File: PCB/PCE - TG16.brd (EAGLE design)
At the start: 58.5 x 60.9 mm, 13 parts, among them U1 SN74AHCT125N, U2 SN74AHCT125N

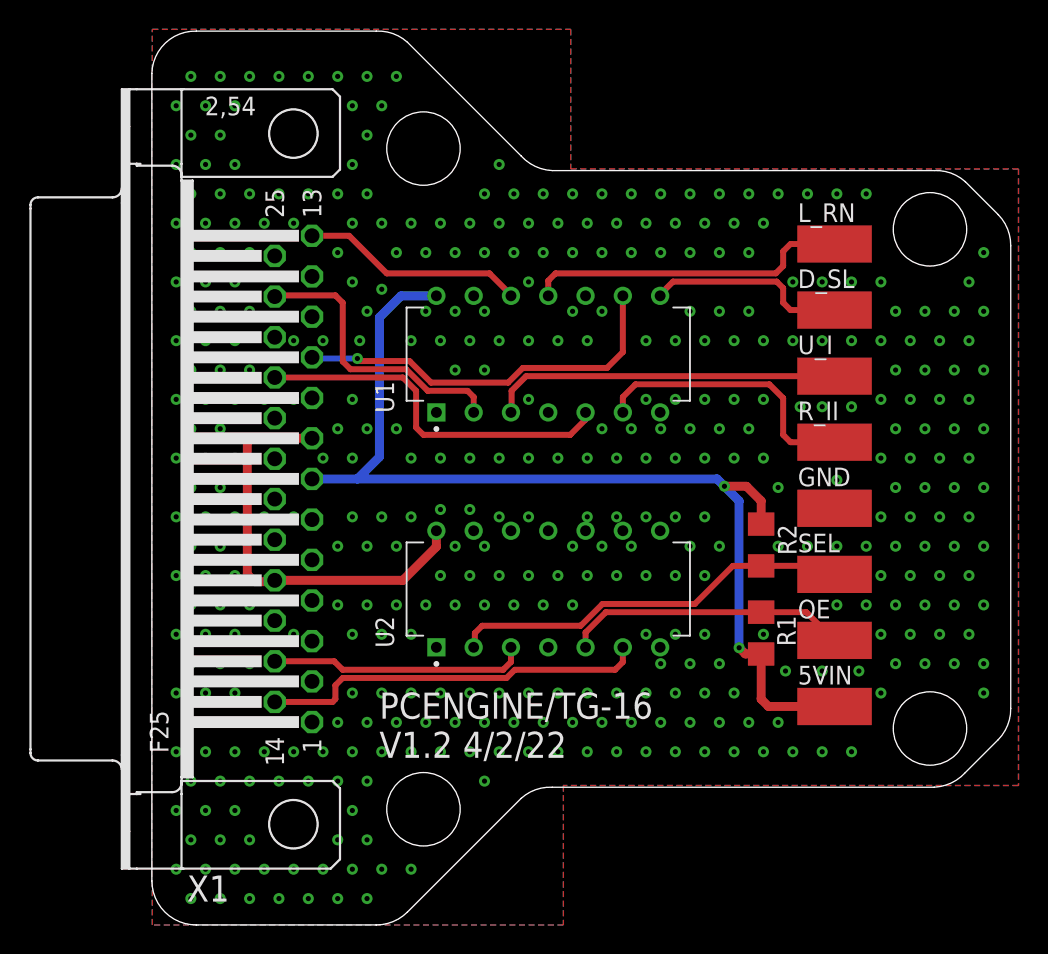
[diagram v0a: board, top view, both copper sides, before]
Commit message: Added exposed GND plane at DB25 anchors
All PCBs have been update to have exposed GND plane pads for the DB25 anchor points.

This resolves Issue 54
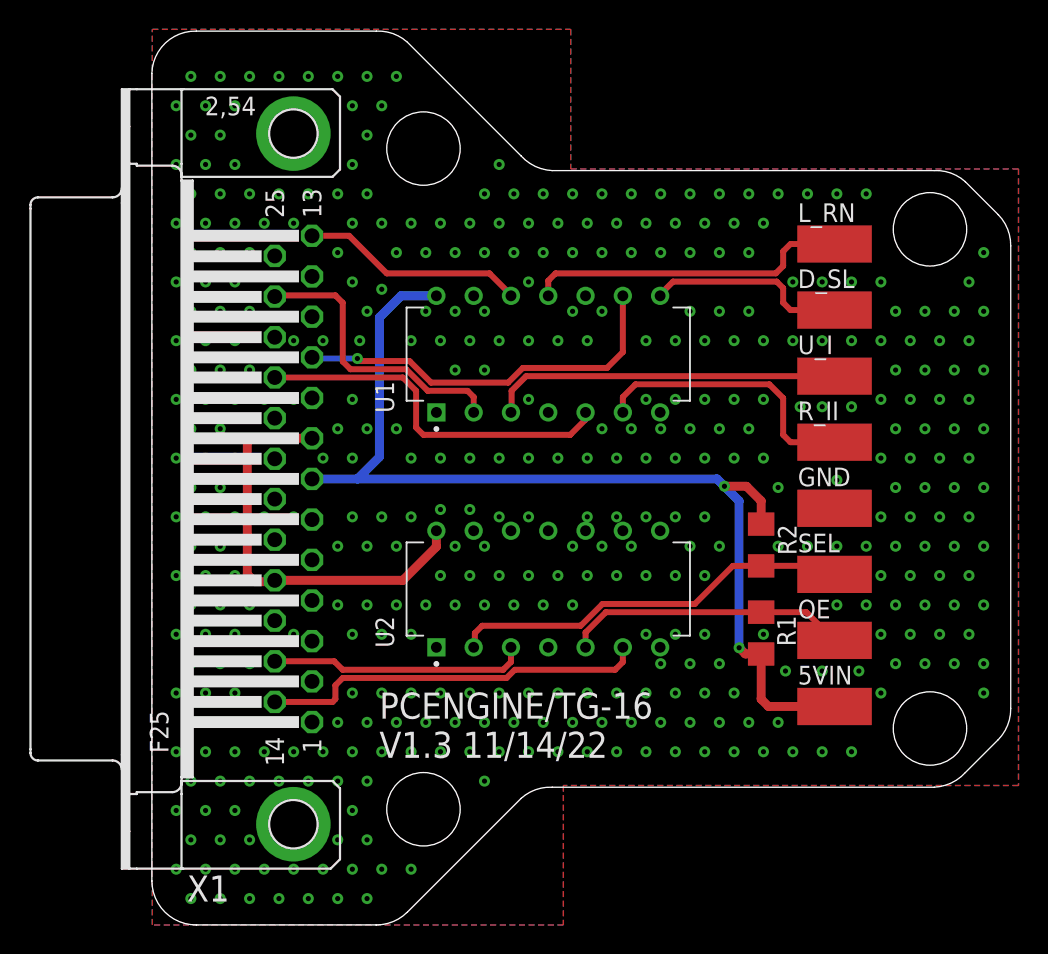
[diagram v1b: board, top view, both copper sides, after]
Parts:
- X1: device SparkFun-Retired:F25H -> SparkFun-Retired:F25HP
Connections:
- net GND: now also X1.GND1, X1.GND2
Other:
- board text added: "PCENGINE/TG-16 V1.3 11/14/22"
- board text removed: "PCENGINE/TG-16 V1.2 4/2/22"
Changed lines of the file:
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@@
 <hole x="18.5" y="8" drill="5"/>
 <text x="15.5" y="11.5" size="1.778" layer="21">PCENGINE/TG-16
-V1.2 4/2/22</text>
+V1.3 11/14/22</text>
 </plain>
 <attributes>
@@
 <attribute name="PURCHASE-URL" value="https://pricing.snapeda.com/search/part/SN74AHCT125N/?ref=eda" x="147.65" y="79.64" size="1.778" layer="27" rot="R90" display="off"/>
 </element>
-<element name="X1" library="SparkFun-Retired" package="F25H" value="" x="9.64" y="30.5" smashed="yes" rot="R90">
+<element name="X1" library="SparkFun-Retired" package="F25HP" value="" x="9.64" y="30.5" smashed="yes" rot="R90">
 <attribute name="NAME" x="5.289" y="3.49" size="1.778" layer="25" ratio="10" rot="R180"/>
 <attribute name="VALUE" x="-4.33" y="22.118" size="1.778" layer="27" ratio="10" rot="R90"/>
@@
 <via x="55.6568" y="43.9168" extent="1-16" drill="0.35"/>
 <via x="56.6568" y="45.9168" extent="1-16" drill="0.35"/>
+<contactref element="X1" pad="GND1"/>
+<contactref element="X1" pad="GND2"/>
 </signal>
 <signal name="5VIN">

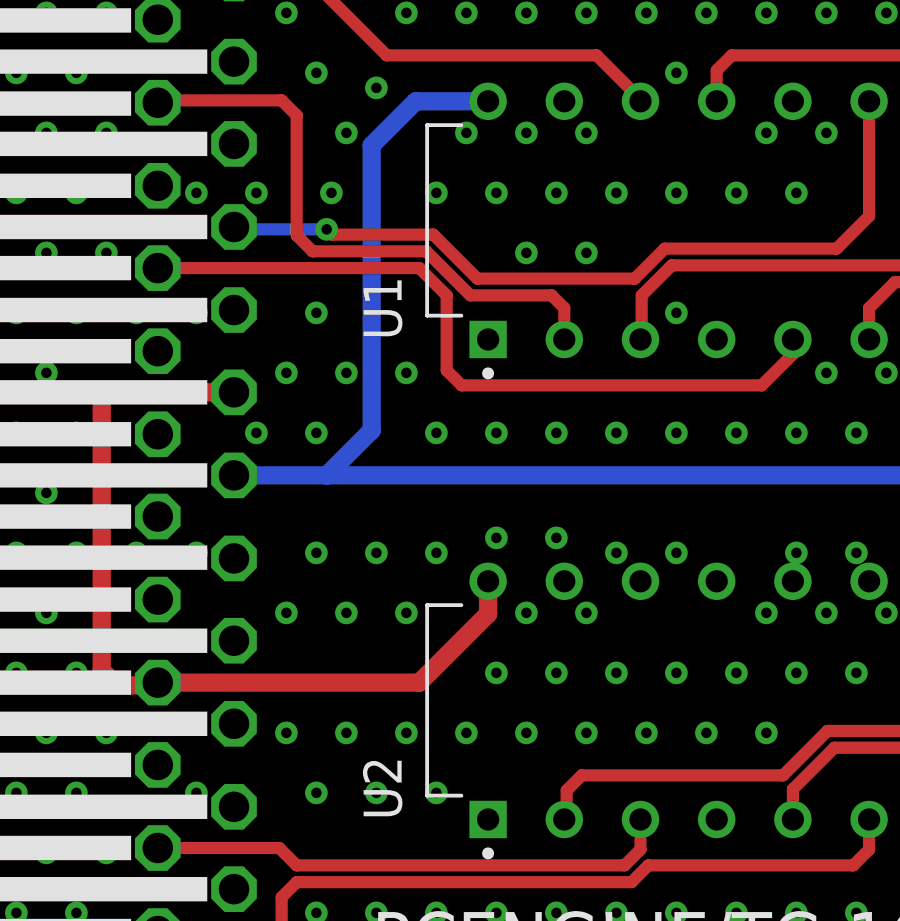
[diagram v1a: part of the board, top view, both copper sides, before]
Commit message: Silkscreen Update, Library Add, Datasheet Add
Updated the silkscreen on all PCBs that used the SN74 components as there was not orientation marker on the silkscreen.

Added Modified SN74 libraries and VB Cable Pinout image
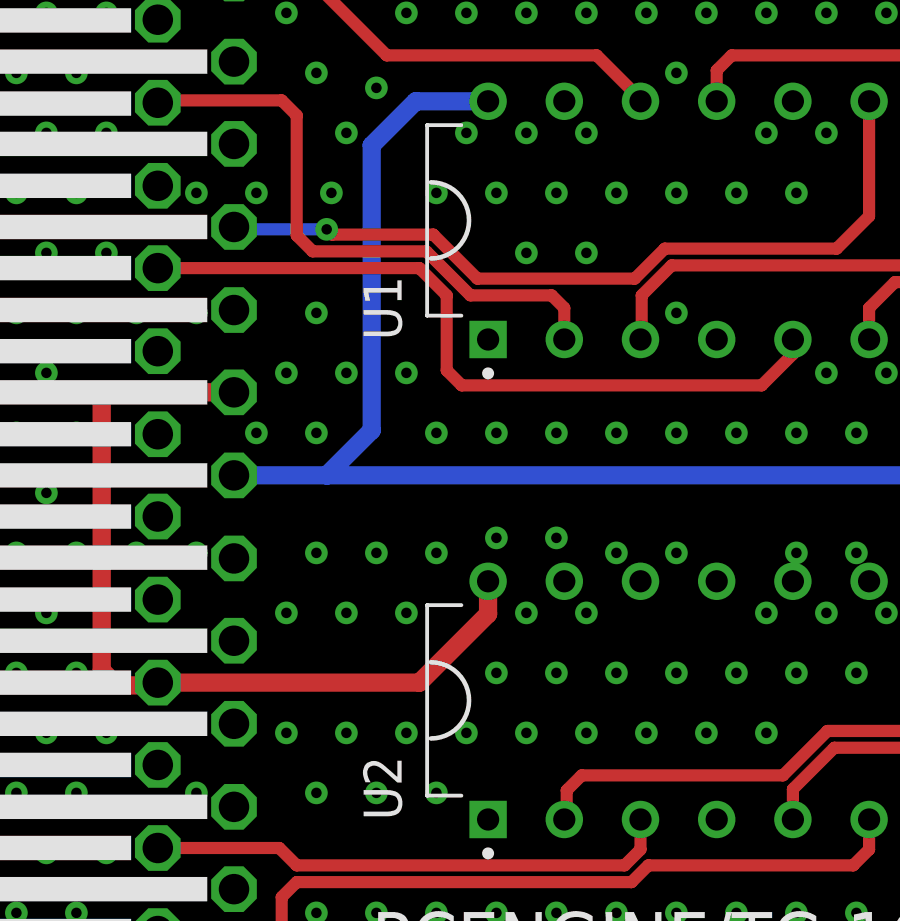
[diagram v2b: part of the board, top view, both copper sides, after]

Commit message: Silkscreen Change (#65)
Added callout to connect cable shield to GND for PCB PCB.  This fixes issues with the 6 button alternate config for the PCE
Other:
- board text added: "CONNECT CABLE SHIELD TO GND"
